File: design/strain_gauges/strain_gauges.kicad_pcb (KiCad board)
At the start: 2 copper layers, 28 parts, among them J1 Conn_01x03, J2 Conn_01x03, J3 Conn_01x08, P1 CONN_01X02, P2 CONN_01X04, P3 CONN_01X04, P4 CONN_01X04, P5 CONN_01X04, Q1 Q_PNP_BCE, U1 LT1460-10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

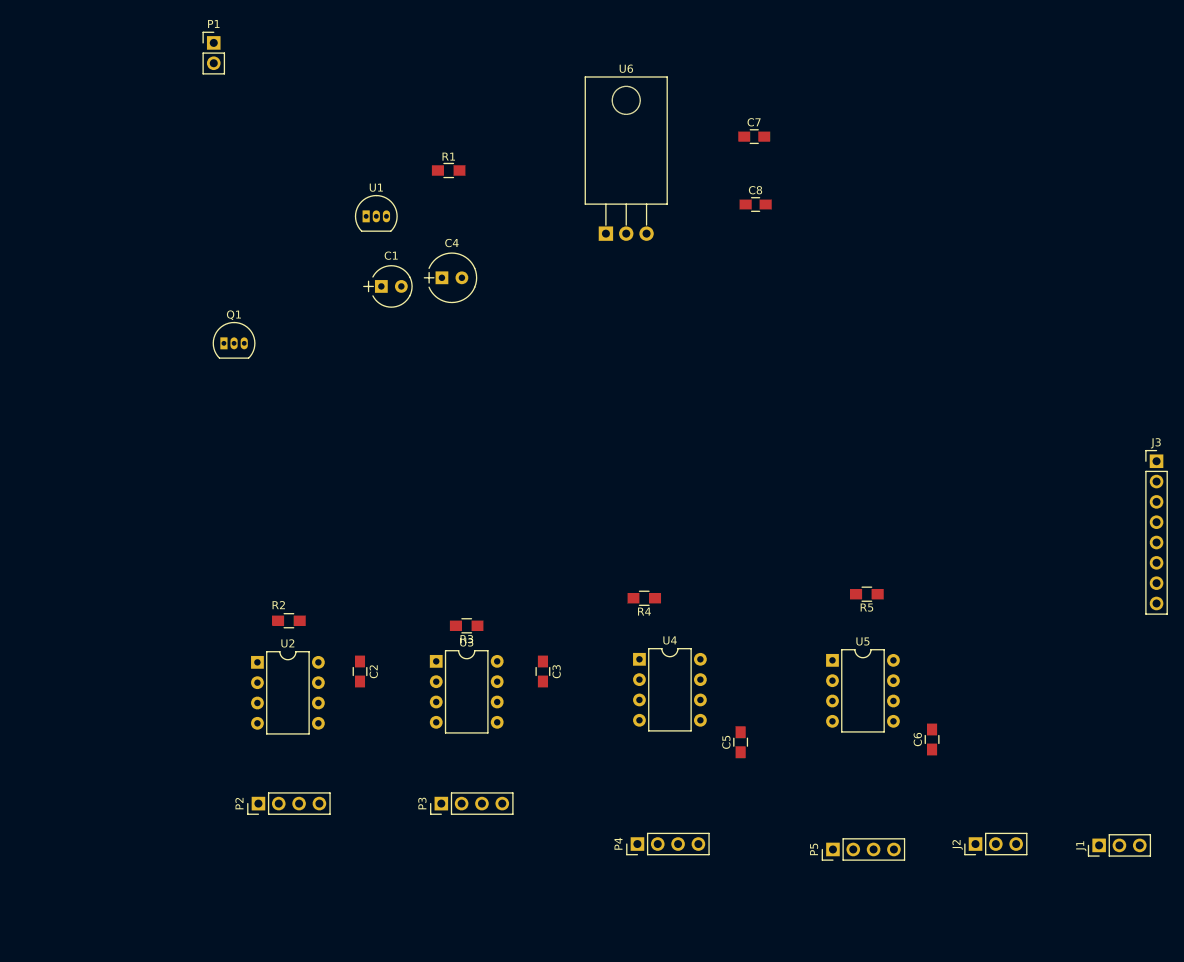
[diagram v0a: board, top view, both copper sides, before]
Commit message: Preliminary board layout (no tracks)
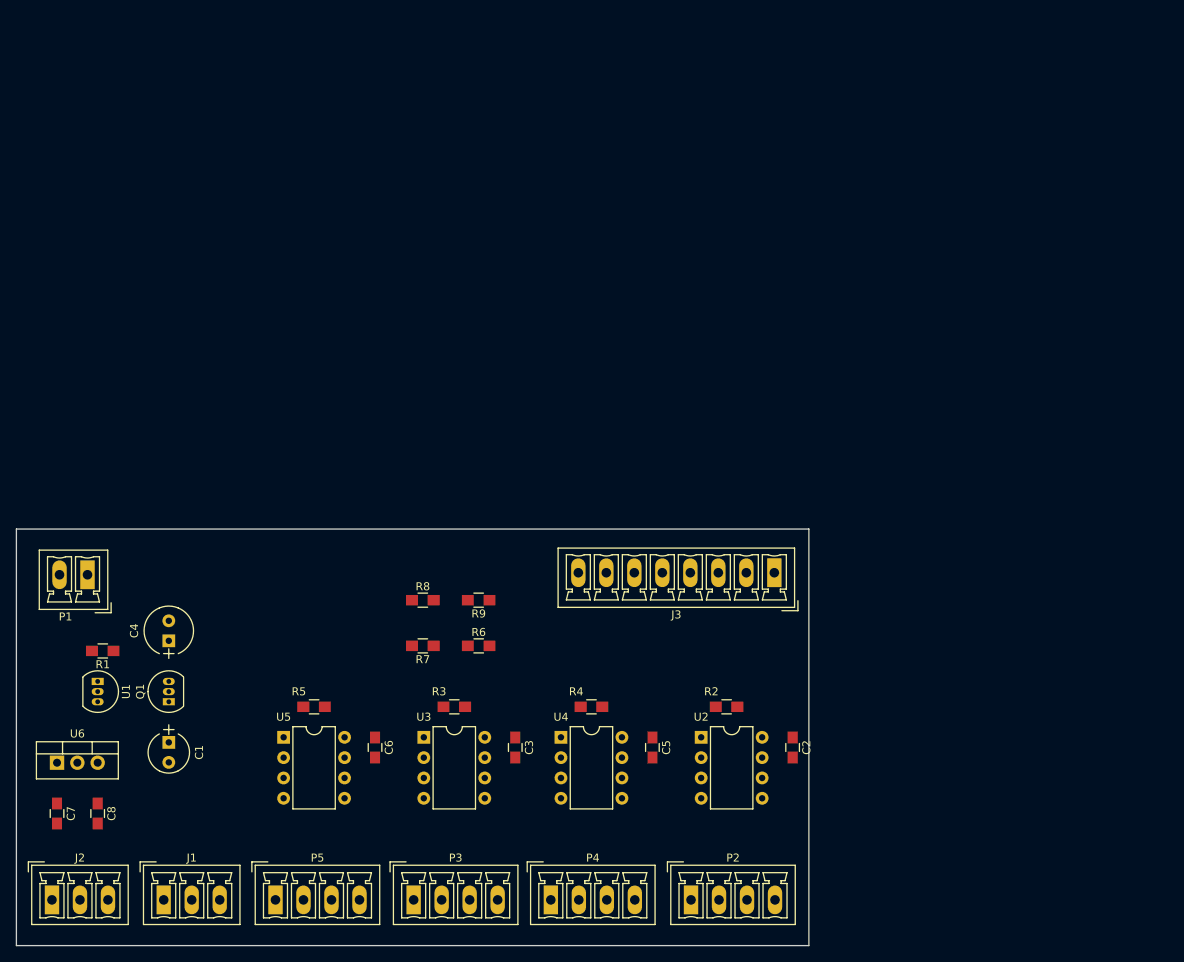
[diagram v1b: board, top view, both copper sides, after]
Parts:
- added R6: 10K, Resistors_SMD:R_0805_HandSoldering, F.Cu at (126.0, 127.0)
- added R7: 10K, Resistors_SMD:R_0805_HandSoldering, F.Cu at (119.0, 127.0)
- added R8: 20K, Resistors_SMD:R_0805_HandSoldering, F.Cu at (119.0, 121.3)
- added R9: 10K, Resistors_SMD:R_0805_HandSoldering, F.Cu at (126.0, 121.3)
- J1, J2: footprint Socket_Strips:Socket_Strip_Straight_1x03_Pitch2.54mm -> Connectors_Phoenix:PhoenixContact_MCV-G_03x3.50mm_Vertical
- J3: footprint Socket_Strips:Socket_Strip_Straight_1x08_Pitch2.54mm -> Connectors_Phoenix:PhoenixContact_MCV-G_08x3.50mm_Vertical
- P1: footprint Socket_Strips:Socket_Strip_Straight_1x02_Pitch2.54mm -> Connectors_Phoenix:PhoenixContact_MCV-G_02x3.50mm_Vertical
- P2, P3, P4, P5: footprint Socket_Strips:Socket_Strip_Straight_1x04_Pitch2.54mm -> Connectors_Phoenix:PhoenixContact_MCV-G_04x3.50mm_Vertical
- Q1: value Q_PNP_BCE -> BC640
- U6: footprint TO_SOT_Packages_THT:TO-220-3_Horizontal -> TO_SOT_Packages_THT:TO-220-3_Vertical
- moved C7 121.5 mm to (73.2, 147.9), turned to 270 degrees
- moved J1 117.1 mm to (86.6, 158.7), turned to 0 degrees
- moved J2 115.7 mm to (72.6, 158.7), turned to 0 degrees
- moved C8 112.1 mm to (78.3, 147.9), turned to 270 degrees
- moved U6 95.3 mm to (73.2, 141.6)
- moved R1 74.0 mm to (79.0, 127.6), turned to 180 degrees
- moved R5 70.5 mm to (105.4, 134.6)
- moved P5 70.0 mm to (100.6, 158.7), turned to 0 degrees
- moved C6 69.6 mm to (113.0, 139.7), turned to 270 degrees
- moved U5 69.3 mm to (101.6, 138.4)
- moved P1 68.3 mm to (77.1, 118.1), turned to 180 degrees
- moved U1 67.1 mm to (78.3, 131.4), turned to 270 degrees
- moved C1 62.9 mm to (87.2, 139.0), turned to 270 degrees
- moved C4 56.8 mm to (87.2, 126.3), turned to 90 degrees
- moved U2 56.3 mm to (153.8, 138.4)
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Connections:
- J3 pad 1: +15V -> STRAIN_OUT_1
- J3 pad 2: +10V -> STRAIN_OUT_2
- J3 pad 3: STRAIN_OUT_1 -> STRAIN_OUT_3
- J3 pad 4: STRAIN_OUT_2 -> STRAIN_OUT_4
- J3 pad 5: STRAIN_OUT_3 -> PRESSURE_1
- J3 pad 6: STRAIN_OUT_4 -> PRESSURE_2
- J3 pad 7: PRESSURE_1 -> Net-(J3-Pad7)
- J3 pad 8: PRESSURE_2 -> Net-(J3-Pad8)
- Q1 pad 1: Net-(Q1-Pad1) -> +10V
- Q1 pad 2: +10V -> +16V
- Q1 pad 3: +16V -> Net-(Q1-Pad3)
- R1 pad 2: Net-(Q1-Pad1) -> Net-(Q1-Pad3)
- U1 pad 1: Net-(Q1-Pad1) -> Net-(Q1-Pad3)
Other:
- board outline added: 99.1 x 52.1 mm

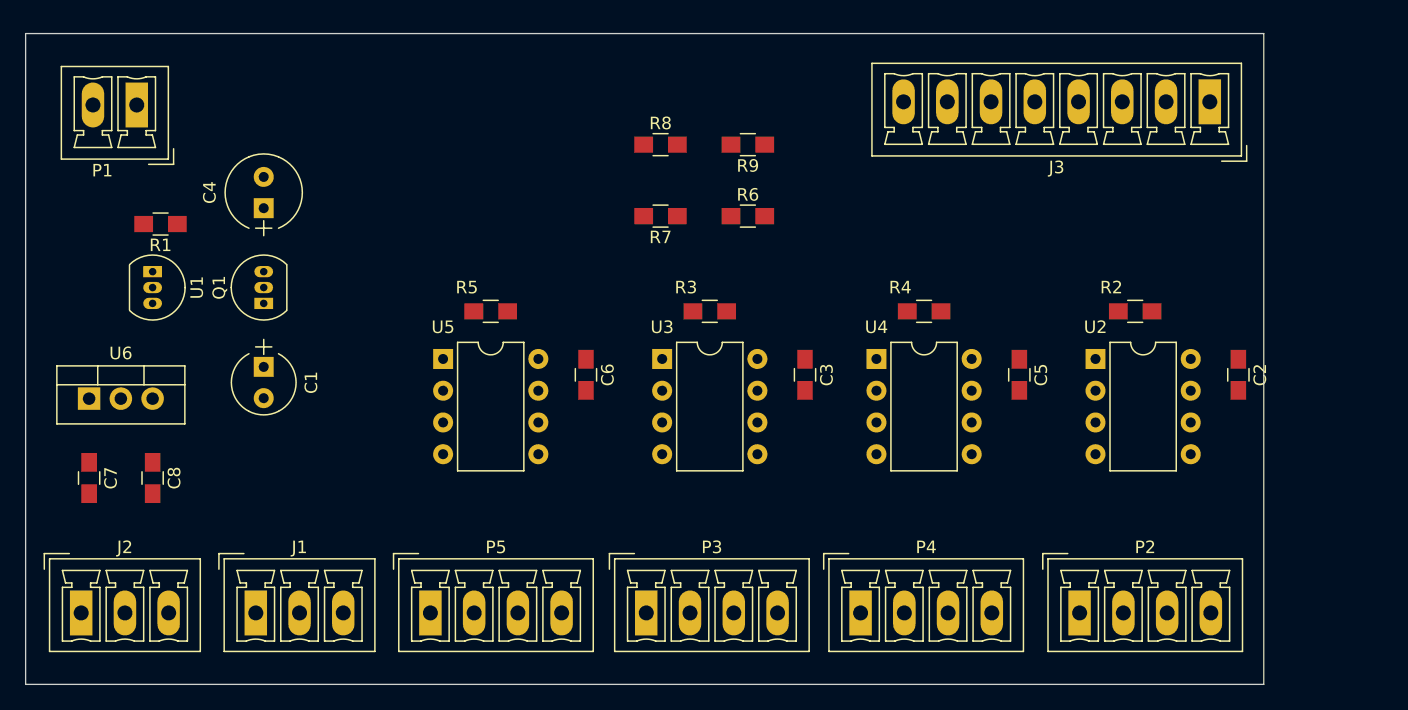
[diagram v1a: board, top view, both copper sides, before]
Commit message: Revised board layout
- move screw terminal locations
- power op amps from 10V line
- misc connector numbering switches
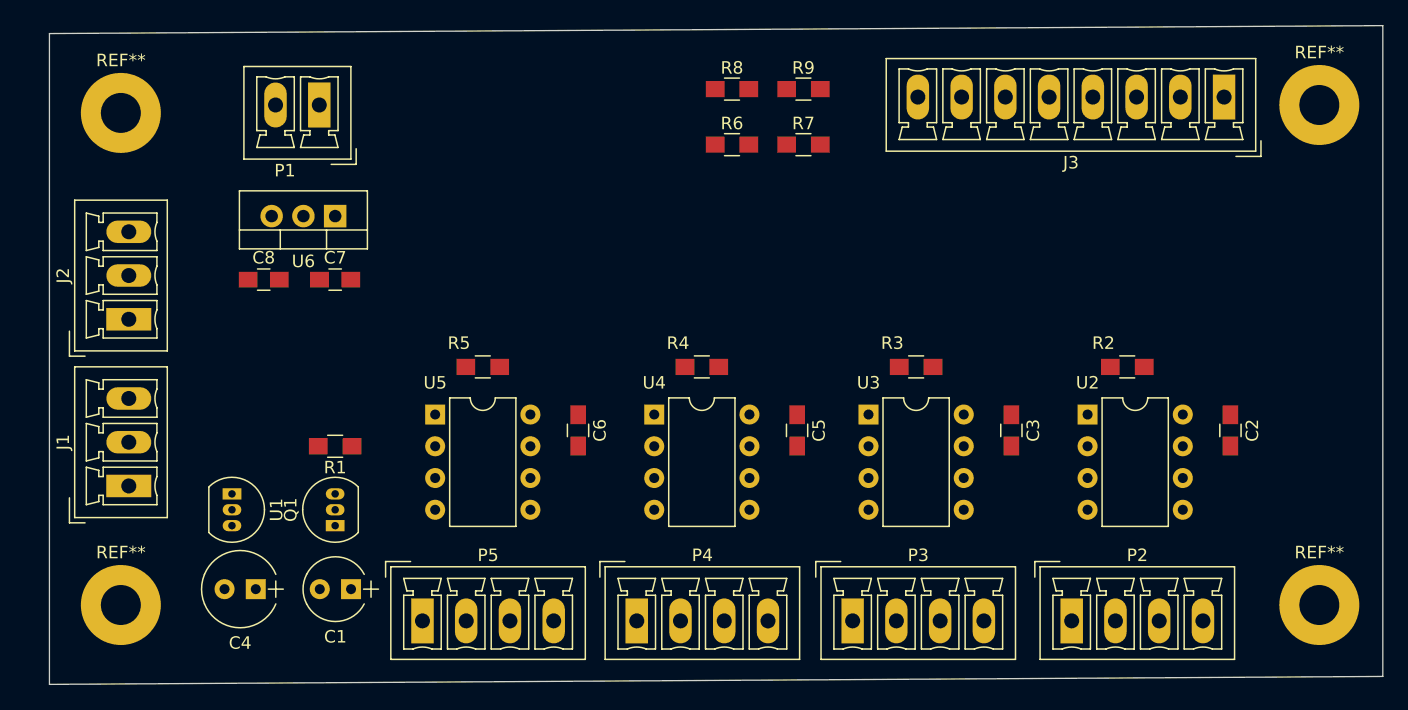
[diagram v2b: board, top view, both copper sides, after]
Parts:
- added REF**: MountingHole_3.2mm_M3_Pad, Mounting_Holes:MountingHole_3.2mm_M3_Pad, F.Cu at (75.8, 158.1)
- added REF**: MountingHole_3.2mm_M3_Pad, Mounting_Holes:MountingHole_3.2mm_M3_Pad, F.Cu at (75.8, 118.7)
- added REF**: MountingHole_3.2mm_M3_Pad, Mounting_Holes:MountingHole_3.2mm_M3_Pad, F.Cu at (171.7, 158.1)
- added REF**: MountingHole_3.2mm_M3_Pad, Mounting_Holes:MountingHole_3.2mm_M3_Pad, F.Cu at (171.7, 118.1)
- moved C4 30.5 mm to (86.6, 156.8), turned to 180 degrees
- moved C7 25.3 mm to (92.9, 132.1), turned to 0 degrees
- moved U6 24.5 mm to (92.9, 127.0), turned to 180 degrees
- moved J2 23.8 mm to (76.4, 135.2), turned to 90 degrees
- moved R1 22.6 mm to (92.9, 145.4)
- moved C1 19.1 mm to (94.2, 156.8), turned to 180 degrees
- moved U1 18.9 mm to (84.7, 149.2)
- moved Q1 18.7 mm to (92.9, 151.7)
- moved C5 18.3 mm to (129.9, 144.1)
- moved R4 18.3 mm to (122.3, 139.0)
- moved U4 18.3 mm to (118.5, 142.8)
- moved C8 18.2 mm to (87.2, 132.1), turned to 0 degrees
- moved P4 17.9 mm to (117.1, 159.4)
- moved C3 17.1 mm to (147.0, 144.1)
- moved R3 17.1 mm to (139.4, 139.0)
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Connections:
- C2 pad 2: +16V -> +10V
- C3 pad 2: +16V -> +10V
- C5 pad 2: +16V -> +10V
- C6 pad 2: +16V -> +10V
- U2 pad 7: +16V -> +10V
- U3 pad 6: STRAIN_OUT_3 -> STRAIN_OUT_2
- U3 pad 7: +16V -> +10V
- U4 pad 6: STRAIN_OUT_2 -> STRAIN_OUT_3
- U4 pad 7: +16V -> +10V
- U5 pad 7: +16V -> +10V
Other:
- board size 99.1 x 52.1 mm -> 106.7 x 52.7 mm

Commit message: Prelim power routing
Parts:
- moved C2 0.64 mm to (164.6, 143.5)
- moved C3 0.64 mm to (147.0, 143.5)
- moved C5 0.64 mm to (129.9, 143.5)
- moved C6 0.64 mm to (112.4, 143.5)
- moved R2 0.63 mm to (156.3, 138.4)
- moved R3 0.63 mm to (139.4, 138.4)
- moved R4 0.63 mm to (122.3, 138.4)
- moved R5 0.63 mm to (104.7, 138.4)
- moved U2 0.63 mm to (153.1, 142.2)
- moved U3 0.63 mm to (135.6, 142.2)
- moved U4 0.63 mm to (118.5, 142.2)
- moved U5 0.63 mm to (100.9, 142.2)
- turned C7 to 180 degrees
- turned C8 to 180 degrees
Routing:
- net +10V: track 0.00 -> 163.3 mm
- net +16V: track 0.00 -> 61.5 mm
- net +15V: track 0.00 -> 36.8 mm
- net Net-(Q1-Pad3): track 0.00 -> 16.2 mm
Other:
- net class Power added: clearance 0.2, trace_width 0.635, via_dia 0.6, via_drill 0.4

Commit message: Prelim power routing
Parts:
- removed P2, P3, P4, P5: CONN_01X04, Connectors_Phoenix:PhoenixContact_MCV-G_04x3.50mm_Vertical
- added J4: Conn_01x04_swapped, Connectors_Phoenix:PhoenixContact_MCV-G_04x3.50mm_Vertical, F.Cu at (152.0, 158.7)
- added J5: Conn_01x04_swapped, Connectors_Phoenix:PhoenixContact_MCV-G_04x3.50mm_Vertical, F.Cu at (134.8, 158.7)
- added J6: Conn_01x04_swapped, Connectors_Phoenix:PhoenixContact_MCV-G_04x3.50mm_Vertical, F.Cu at (117.7, 158.7)
- added J7: Conn_01x04_swapped, Connectors_Phoenix:PhoenixContact_MCV-G_04x3.50mm_Vertical, F.Cu at (100.6, 158.7)
- moved R2 0.76 mm to (157.1, 138.4)
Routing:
- net +10V: track 163.3 -> 174.8 mm
- net Net-(R3-Pad1): track 0.00 -> 5.82 mm
- net Net-(R4-Pad1): track 0.00 -> 5.82 mm
- net Net-(R5-Pad2): track 0.00 -> 5.75 mm
- net Net-(R5-Pad1): track 0.00 -> 5.67 mm
- net Net-(R3-Pad2): track 0.00 -> 5.60 mm
- net Net-(R4-Pad2): track 0.00 -> 5.60 mm
- net Net-(R2-Pad2): track 0.00 -> 5.58 mm
- net Net-(R2-Pad1): track 0.00 -> 5.47 mm
- net Net-(Q1-Pad3): track 16.2 -> 18.1 mm, vias 0 -> 1
- net +16V: track 61.5 -> 60.6 mm, vias 0 -> 1
- net +15V: track 36.8 -> 37.4 mm

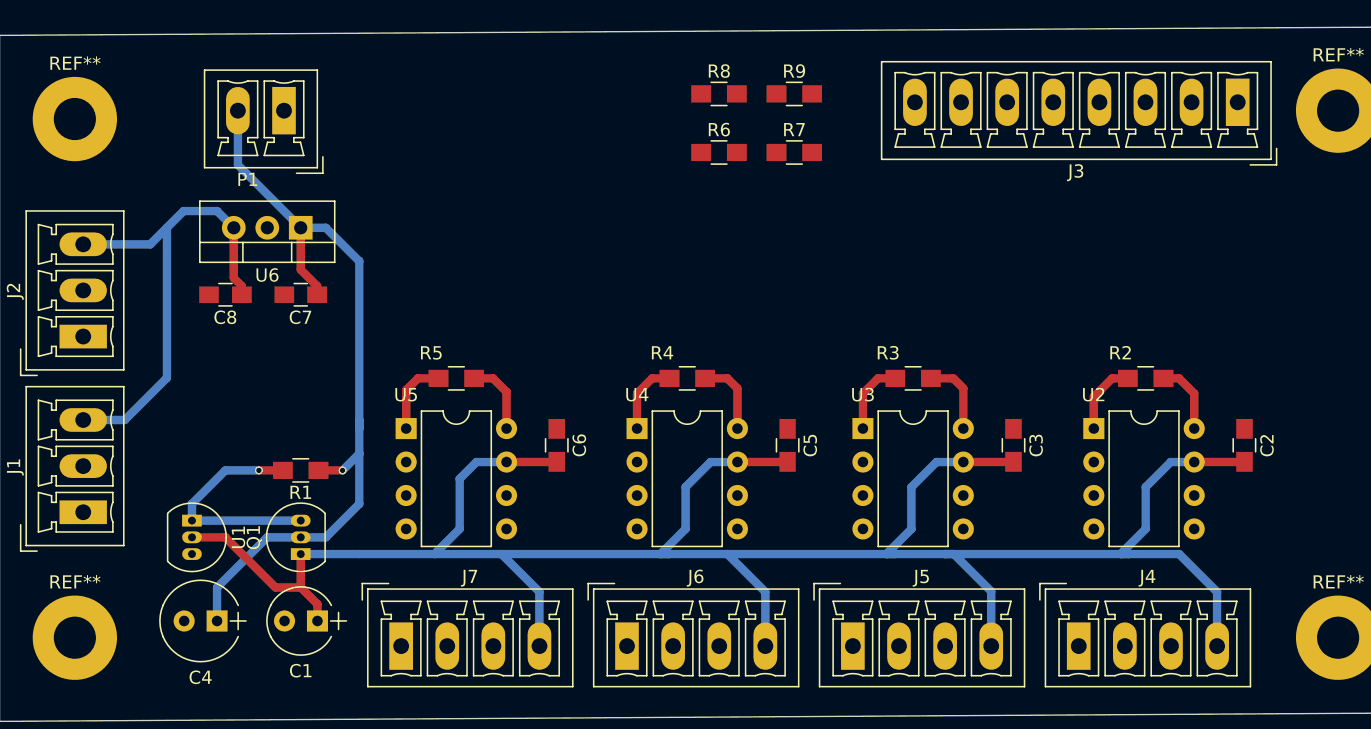
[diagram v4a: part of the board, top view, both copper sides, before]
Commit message: First pass board routing
- will probably go back and change placement of power blocks
- likely not final
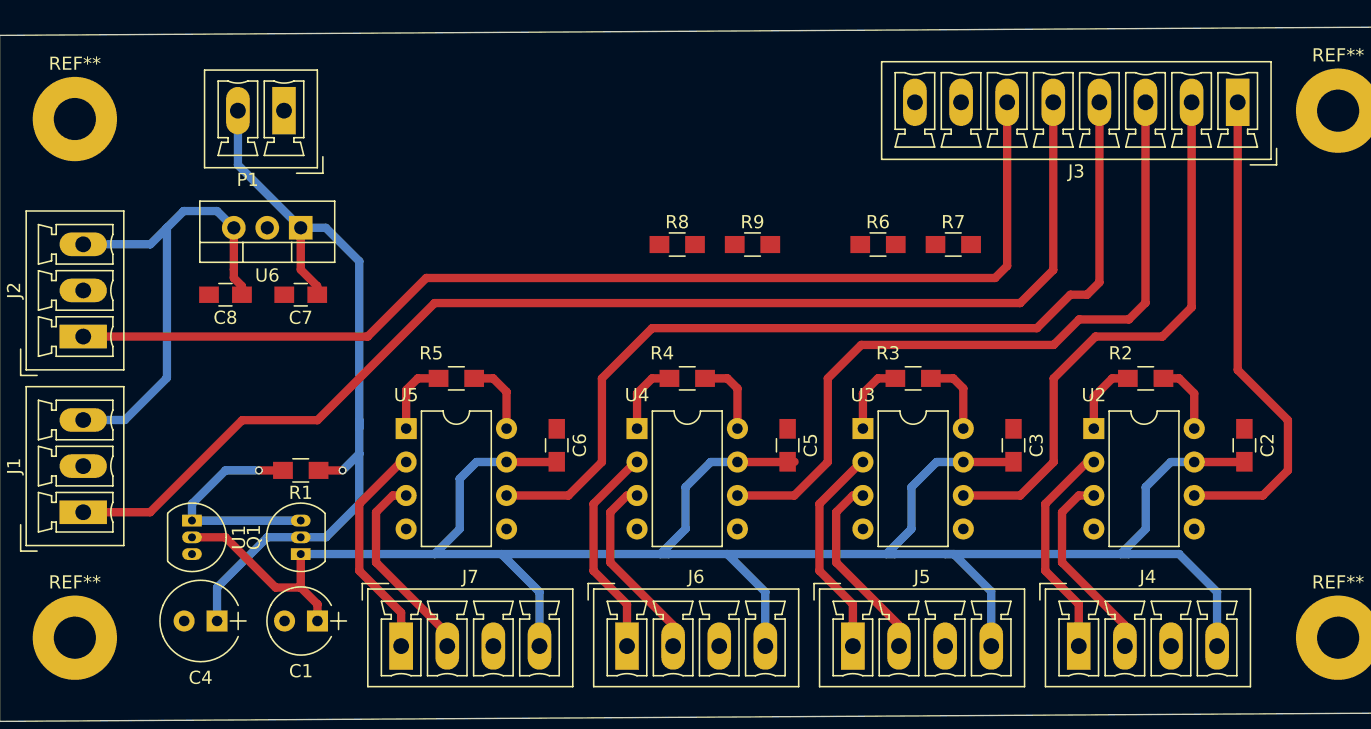
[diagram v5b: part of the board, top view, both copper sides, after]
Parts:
- moved R6 13.9 mm to (136.8, 128.2)
- moved R7 13.9 mm to (142.5, 128.2)
- moved R9 11.9 mm to (127.2, 128.2)
- moved R8 11.9 mm to (121.5, 128.2)
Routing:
- net PRESSURE_1: track 0.00 -> 94.0 mm
- net PRESSURE_2: track 0.00 -> 84.8 mm
- net STRAIN_OUT_4: track 0.00 -> 69.1 mm
- net STRAIN_OUT_3: track 0.00 -> 56.0 mm
- net STRAIN_OUT_2: track 0.00 -> 42.5 mm
- net STRAIN_OUT_1: track 0.00 -> 37.4 mm
- net Net-(J7-Pad1): track 0.00 -> 17.0 mm
- net Net-(J4-Pad1): track 0.00 -> 16.8 mm
- net Net-(J6-Pad1): track 0.00 -> 16.5 mm
- net Net-(J5-Pad1): track 0.00 -> 16.5 mm
- net Net-(J7-Pad2): track 0.00 -> 15.2 mm
- net Net-(J4-Pad2): track 0.00 -> 15.1 mm
- net Net-(J5-Pad2): track 0.00 -> 14.7 mm
- net Net-(J6-Pad2): track 0.00 -> 14.7 mm
- net +10V: track 174.8 -> 175.3 mm
